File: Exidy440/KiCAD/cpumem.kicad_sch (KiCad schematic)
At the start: 58 parts, among them P1 50 PIN RIBBON CABLE, P2 Gun Connector, SW1 DIP SWITCH, U10A HM6116P-3, U11J 74LS02, U12A 74LS245, U12J 74LS245, U13A 74LS245, U13J 74LS273, U14J 74LS374, U15J 74LS374, U16J 74LS244, U17J 74LS374, U18J 74LS244, U1A 2764, U1H MC6809E, U1K NE555P, U21J 74LS00, U22J 74LS20, U23J 74LS74, U2F 74LS244, U2H LS287, U2J 74LS05, U2K 74LS112, U2L 74LS04, U3A 2764, U3H 74LS138, U3J 74LS10, U4A 2764, U4F 74LS244, U4H 74LS138, U4J 74LS138, U5H 74LS32, U5J 74LS04, U6A 2764, U6H 74LS04, U7A 2764, U8A HM6116P-3

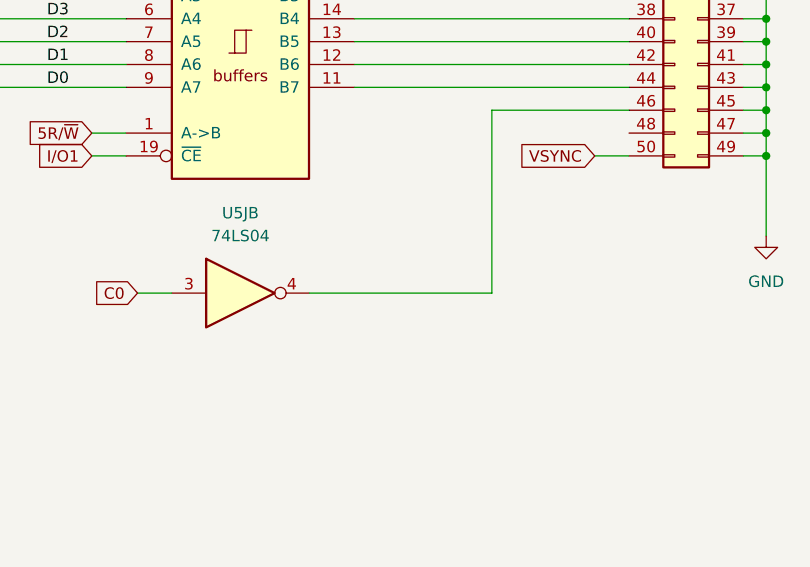
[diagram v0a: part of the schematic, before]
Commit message: Misc fixes found while checking clocks in FPGA core
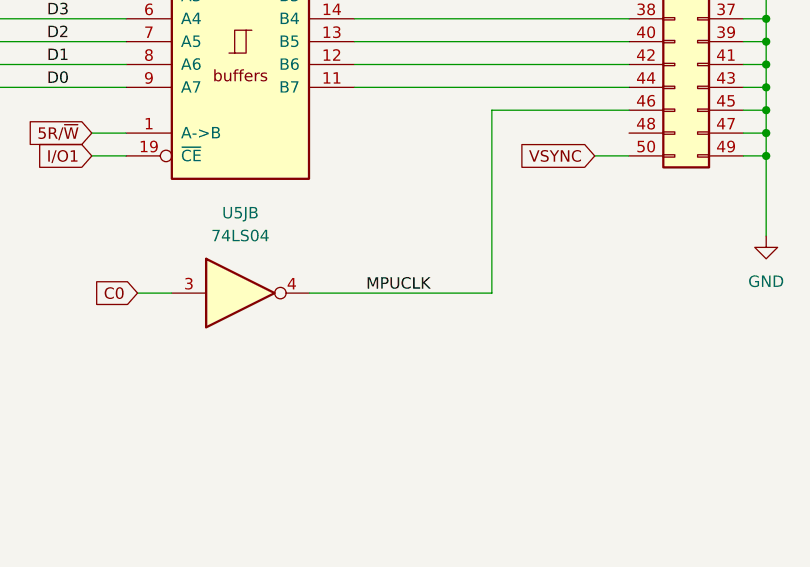
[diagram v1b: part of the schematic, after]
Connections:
- net MPUCLK: now reaches P1.46 (Pin_46), U5J.4
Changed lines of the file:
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@@
+		)
+	)
+	(label "MPUCLK"
+		(at 492.76 379.73 0)
+		(effects
+			(font
+				(size 1.27 1.27)
+			)
+			(justify left bottom)
 		)
 	)

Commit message: Added dual PCB structure, misc fixes and start of audio board IO
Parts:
- renumbered C2 to C?, C4 to C?, C3 to C?, CR1 to CR?, E2 to E?, P1 to P?, P2 to P?, R11 to R?, R12 to R?, R13 to R?, R6 to R?, R9 to R?, R7 to R?, R4 to R?, R20 to R?, R5 to R?, R10 to R?, R8 to R?, SW1 to SW?, U10A to U10A?, U11J to U11J?, U12A to U12A?, U12J to U12J?, U13A to U13A?, U13J to U13J?, U14J to U14J?, U15J to U15J?, U16J to U16J?, U17J to U17J?, U18J to U18J?, U1A to U1A?, U1H to U1H?, U1K to U1K?, U21J to U21J?, U22J to U22J?, U23J to U23J?, U2F to U2F?, U2H to U2H?, U2J to U2J?, U2K to U2K?, U2L to U2L?, U3A to U3A?, U3H to U3H?, U3J to U3J?, U4A to U4A?, U4F to U4F?, U4H to U4H?, U4J to U4J?, U5H to U5H?, U5J to U5J?, U6A to U6A?, U6H to U6H?, U7A to U7A?, U8A to U8A?, UJ21 to UJ?

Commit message: Correction of references after copy/paste issue.  Additional IO on audio board.
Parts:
- gave numbers to parts that had none: 58
